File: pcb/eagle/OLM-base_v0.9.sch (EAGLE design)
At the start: 33 parts, among them IC1 ATMEGA, IC2 MCP1702-33, IC3 ENC28J60SP, J1 MAGJACK, J2 POWER_JACKPTH, X1 16 MHz, X3 25MHz

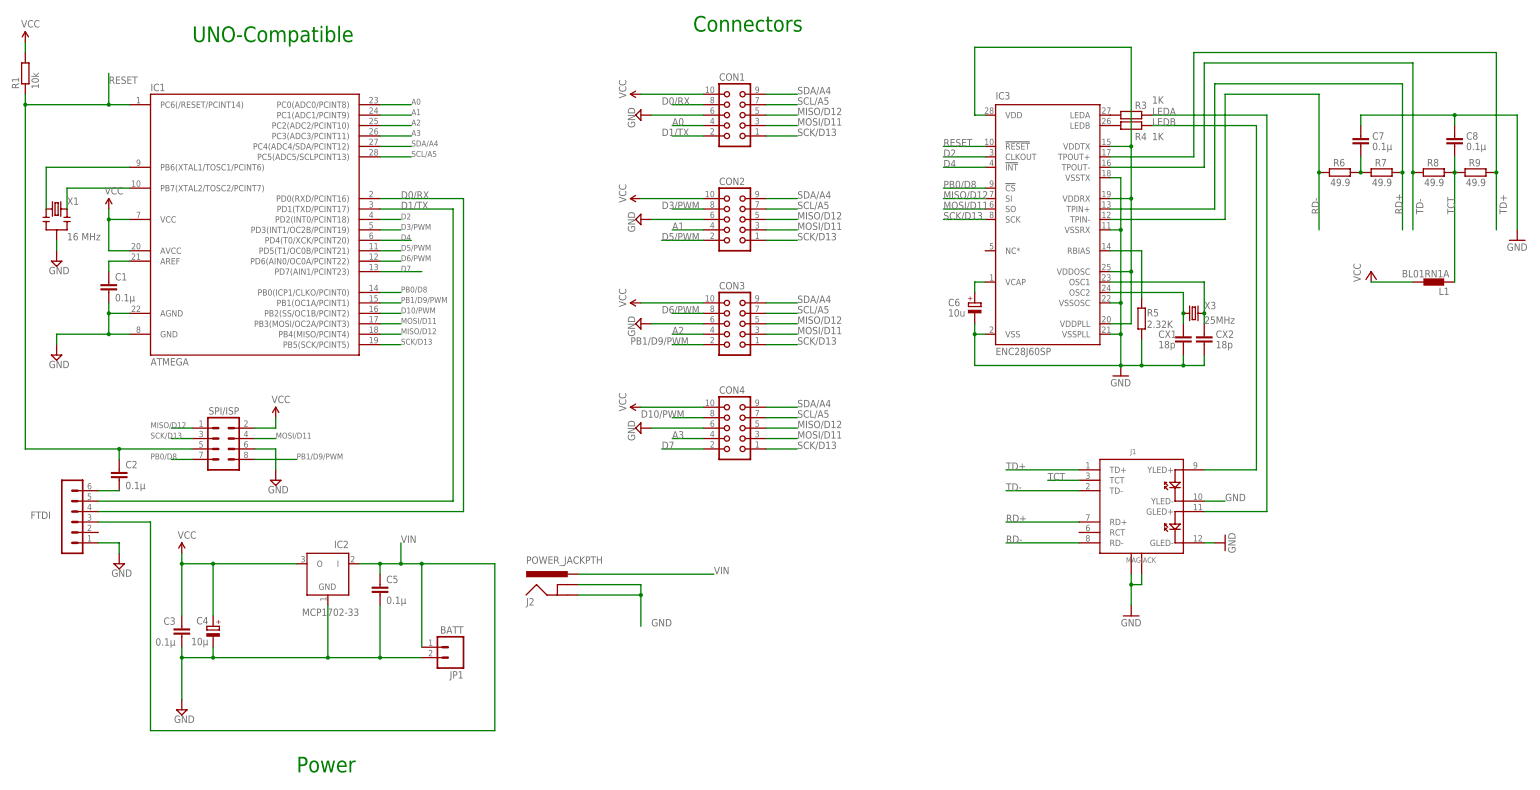
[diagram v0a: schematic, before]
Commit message: fixed logo
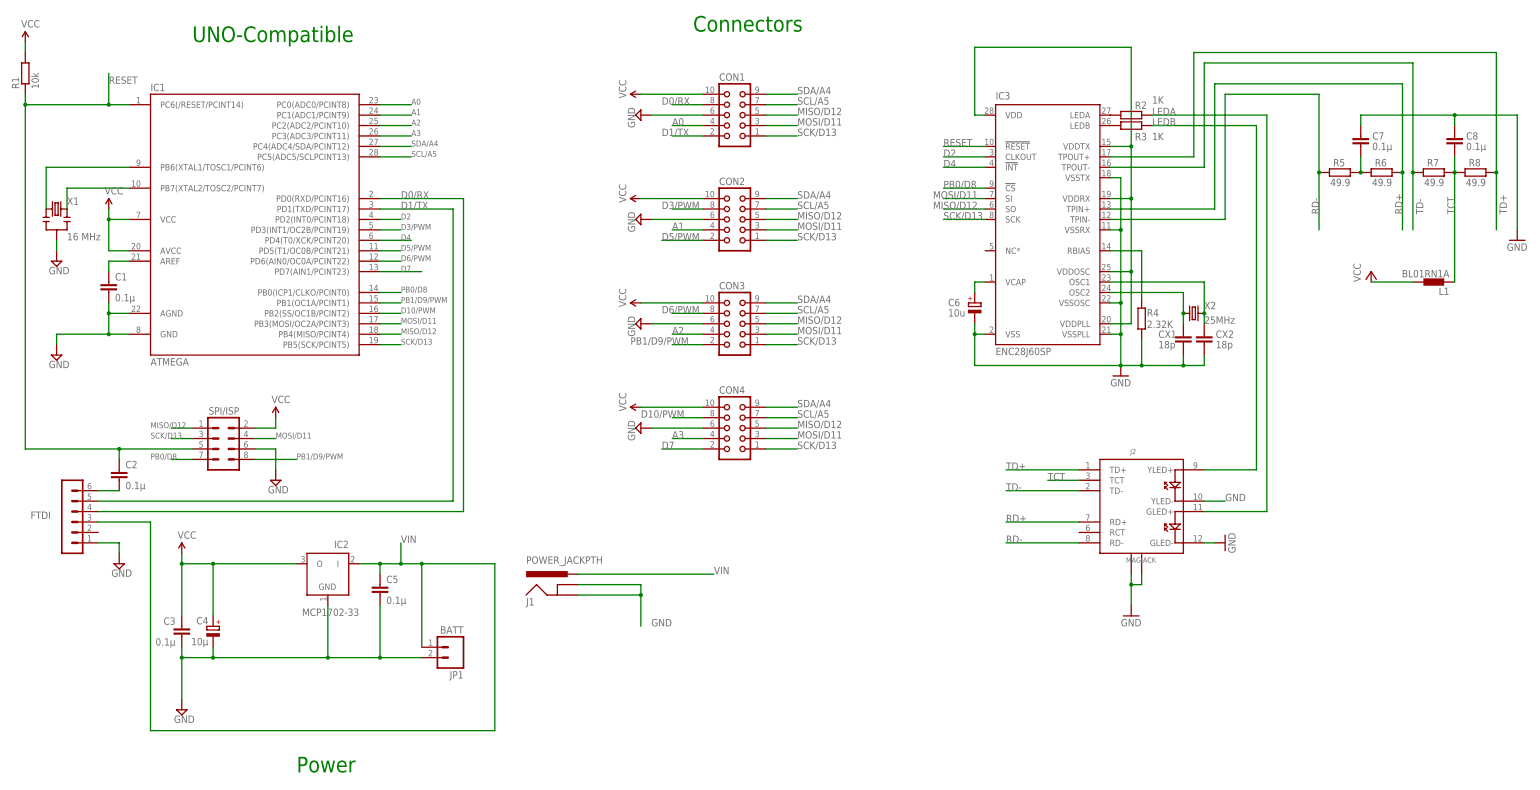
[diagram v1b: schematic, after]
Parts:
- removed R9: 49.9, rcl:R-EU_0204/7
- added R2: 1K, rcl:R-EU_0204/7
- J1: value MAGJACK -> POWER_JACKPTH; device SparkFun:MAGJACK -> SparkFun-Connectors:POWER_JACKPTH
- J2: value POWER_JACKPTH -> MAGJACK; device SparkFun-Connectors:POWER_JACKPTH -> SparkFun:MAGJACK
- R4: value 1K -> 2.32K
- R5: value 2.32K -> 49.9
- renumbered X3 to X2
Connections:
- net GND: now also J1.GND, J1.GNDBREAK, J2.GLED-, J2.GND1, J2.GND2, J2.YLED-, R4.2; no longer J1.GLED-, J1.GND1, J1.GND2, J1.YLED-, J2.GND, J2.GNDBREAK, R5.2
- net LEDA: now also J2.GLED+, R2.2; no longer J1.GLED+, R3.2
- net LEDB: now also J2.YLED+, R3.2; no longer J1.YLED+, R4.2
- net MISO/D12: now also IC3.SO; no longer IC3.SI
- net MOSI/D11: now also IC3.SI; no longer IC3.SO
- net N$37: now also R2.1; no longer R3.1
- net N$39: now also R3.1; no longer R4.1
- net N$51: now also R4.1; no longer R5.1
- net N$54: now also R5.2, R6.1; no longer R6.2, R7.1
- net RD+: now also J2.RD+, R6.2; no longer J1.RD+, R7.2
- net RD-: now also J2.RD-, R5.1; no longer J1.RD-, R6.1
- net TCT: now also J2.TCT, R7.2, R8.1; no longer J1.TCT, R8.2, R9.1
- net TD+: now also J2.TD+, R8.2; no longer J1.TD+, R9.2
- net TD-: now also J2.TD-, R7.1; no longer J1.TD-, R8.1
- net VIN: now also J1.PWR; no longer J2.PWR
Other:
- moved on the sheet: R3, R4, R5, R6, R7, R8
